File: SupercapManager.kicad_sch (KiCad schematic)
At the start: 0 parts

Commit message: Add subsheets
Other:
- added sheet Current Sense (isense.kicad_sch)
- added sheet Input Buck & Charger (buck.kicad_sch)
- added sheet Output Boost (boost.kicad_sch)
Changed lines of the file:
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@@
 		(comment 1 "Robomaster")
+	)
+	(sheet
+		(at 81.28 97.79)
+		(size 25.4 15.24)
+		(fields_autoplaced yes)
+		(stroke
+			(width 0.1524)
+			(type solid)
+		)
+		(fill
+			(color 0 0 0 0.0000)
+		)
+		(property "Sheetname" "Input Buck & Charger"
+			(at 81.28 97.0784 0)
+			(effects
+				(font
+					(size 1.27 1.27)
+				)
+				(justify left bottom)
+			)
+		)
+		(property "Sheetfile" "buck.kicad_sch"
+			(at 81.28 113.6146 0)
+			(effects
+				(font
+					(size 1.27 1.27)
+				)
+				(justify left top)
+			)
+		)
+		(instances
+			(project "SupercapManager"
+				(path "/6197145b-e7d4-44cc-9d90-537b6501bf60"
+					(page "2")
+				)
+			)
+		)
+	)
+	(sheet
+		(at 118.11 73.66)
+		(size 26.67 12.7)
+		(fields_autoplaced yes)
+		(stroke
+			(width 0.1524)
+			(type solid)
+		)
+		(fill
+			(color 0 0 0 0.0000)
+		)
+		(property "Sheetname" "Current Sense"
+			(at 118.11 72.9484 0)
+			(effects
+				(font
+					(size 1.27 1.27)
+				)
+				(justify left bottom)
+			)
+		)
+		(property "Sheetfile" "isense.kicad_sch"
+			(at 118.11 86.9446 0)
+			(effects
+				(font
+					(size 1.27 1.27)
+				)
+				(justify left top)
+			)
+		)
+		(instances
+			(project "SupercapManager"
+				(path "/6197145b-e7d4-44cc-9d90-537b6501bf60"
+					(page "4")
+				)
+			)
+		)
+	)
+	(sheet
+		(at 162.56 97.79)
+		(size 26.67 15.24)
+		(fields_autoplaced yes)
+		(stroke
+			(width 0.1524)
+			(type solid)
+		)
+		(fill
+			(color 0 0 0 0.0000)
+		)
+		(property "Sheetname" "Output Boost"
+			(at 162.56 97.0784 0)
+			(effects
+				(font
+					(size 1.27 1.27)
+				)
+				(justify left bottom)
+			)
+		)
+		(property "Sheetfile" "boost.kicad_sch"
+			(at 162.56 113.6146 0)
+			(effects
+				(font
+					(size 1.27 1.27)
+				)
+				(justify left top)
+			)
+		)
+		(instances
+			(project "SupercapManager"
+				(path "/6197145b-e7d4-44cc-9d90-537b6501bf60"
+					(page "3")
+				)
+			)
+		)
 	)
 	(sheet_instances

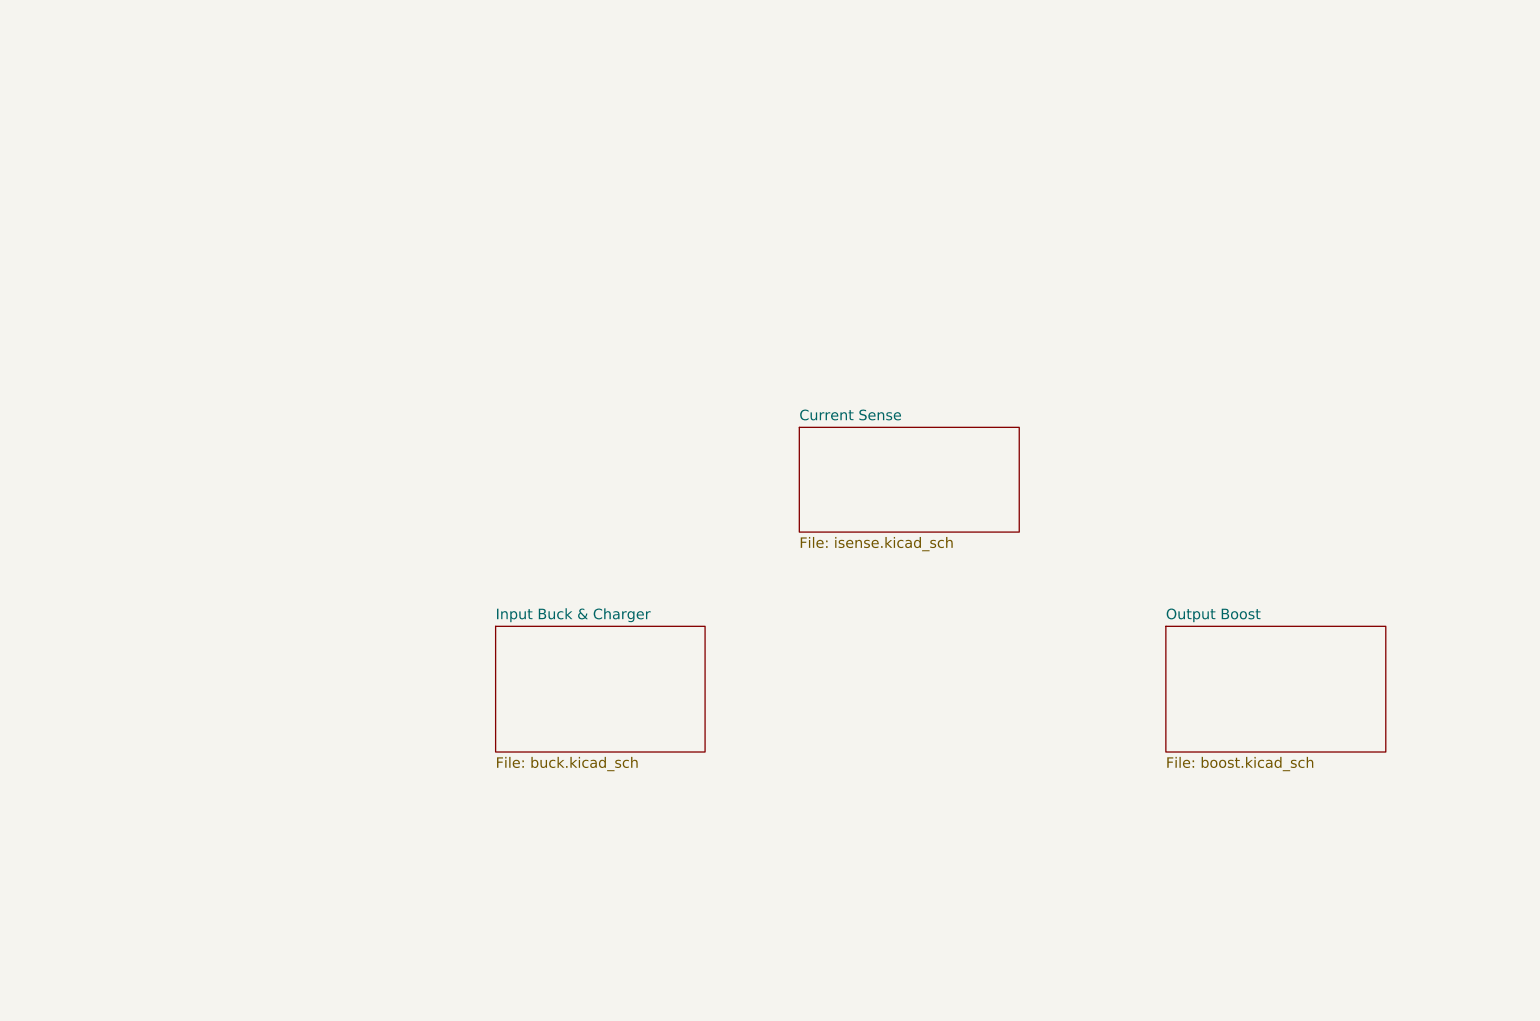
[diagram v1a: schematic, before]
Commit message: Added some text in the subsheets to outline what needs to be added inside of each subsheet
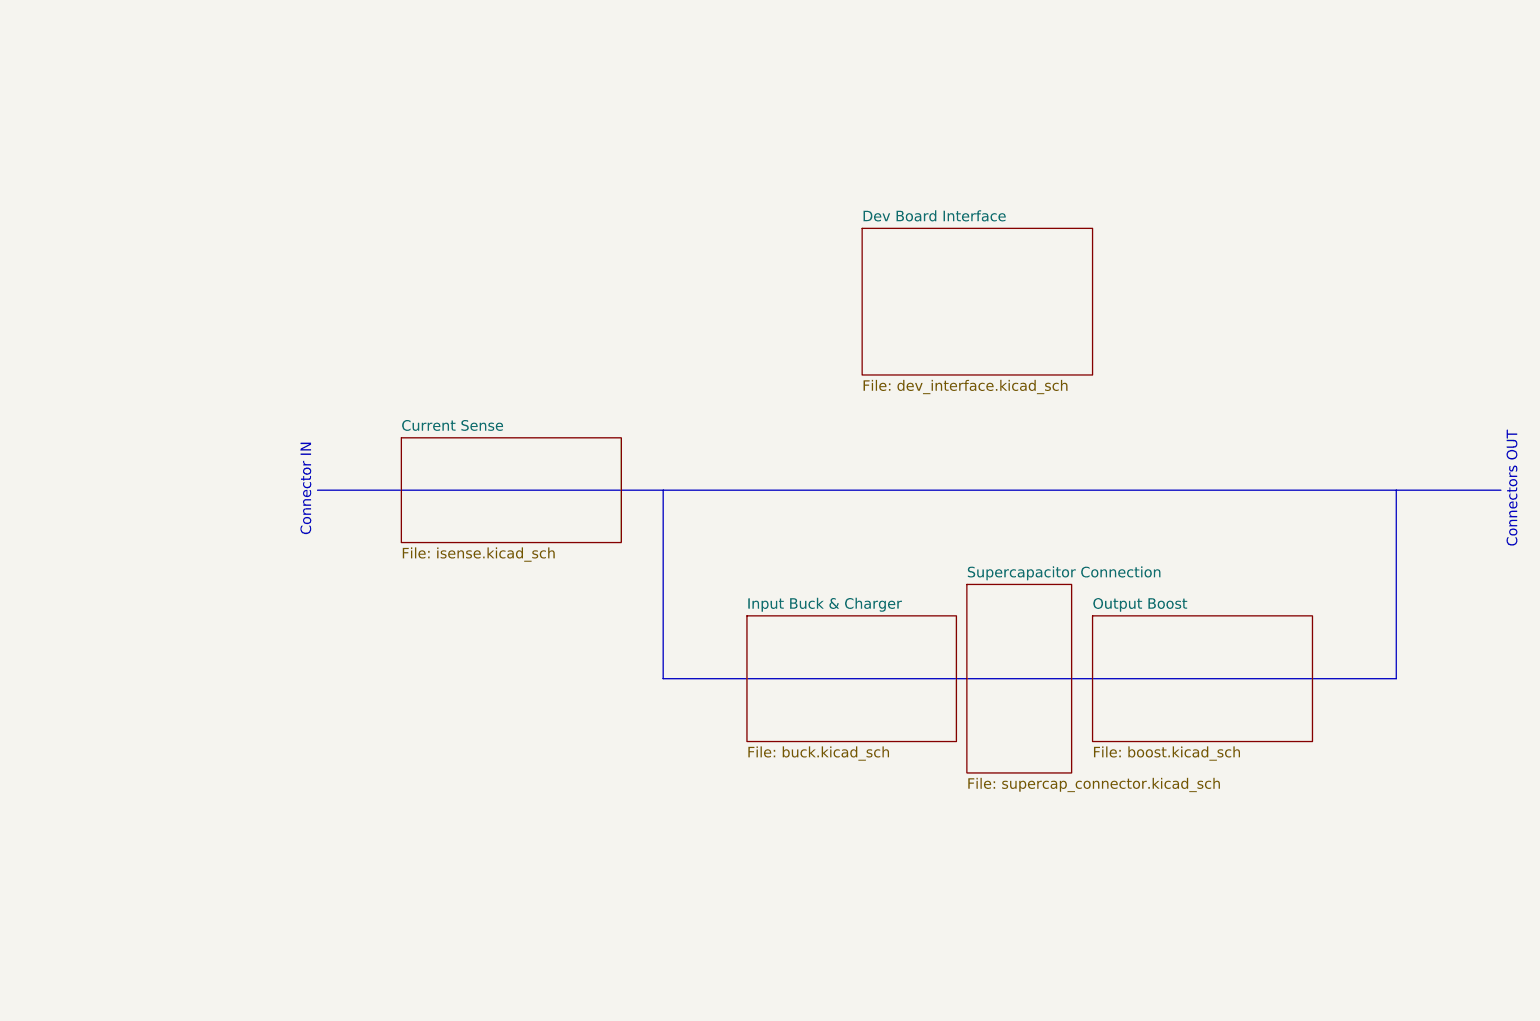
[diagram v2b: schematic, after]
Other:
- added sheet Dev Board Interface (dev_interface.kicad_sch)
- added sheet Supercapacitor Connection (supercap_connector.kicad_sch)
- note added: "Connector IN"
- note added: "Connectors OUT"
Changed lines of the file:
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@@
 		(comment 1 "Robomaster")
 	)
-	(sheet
-		(at 81.28 97.79)
+	(polyline
+		(pts
+			(xy 101.6 81.28) (xy 101.6 104.14)
+		)
+		(stroke
+			(width 0)
+			(type default)
+		)
+	)
+	(polyline
+		(pts
+			(xy 101.6 104.14) (xy 190.5 104.14)
+		)
+		(stroke
+			(width 0)
+			(type default)
+		)
+	)
+	(polyline
+		(pts
+			(xy 59.69 81.28) (xy 203.2 81.28)
+		)
+		(stroke
+			(width 0)
+			(type default)
+		)
+	)
+	(polyline
+		(pts
+			(xy 190.5 104.14) (xy 190.5 81.28)
+		)
+		(stroke
+			(width 0)
+			(type default)
+		)
+	)
+	(text "Connector IN"
+		(exclude_from_sim no)
+		(at 59.055 81.28 90)
+		(effects
+			(font
+				(size 1.27 1.27)
+			)
+			(justify bottom)
+		)
+	)
+	(text "Connectors OUT"
+		(exclude_from_sim no)
+		(at 203.835 81.28 90)
+		(effects
+			(font
+				(size 1.27 1.27)
+			)
+			(justify top)
+		)
+	)
+	(sheet
+		(at 125.73 49.53)
+		(size 27.94 17.78)
+		(fields_autoplaced yes)
+		(stroke
+			(width 0.1524)
+			(type solid)
+		)
+		(fill
+			(color 0 0 0 0.0000)
+		)
+		(property "Sheetname" "Dev Board Interface"
+			(at 125.73 48.8184 0)
+			(effects
+				(font
+					(size 1.27 1.27)
+				)
+				(justify left bottom)
+			)
+		)
+		(property "Sheetfile" "dev_interface.kicad_sch"
+			(at 125.73 67.8946 0)
+			(effects
+				(font
+					(size 1.27 1.27)
+				)
+				(justify left top)
+			)
+		)
+		(instances
+			(project "SupercapManager"
+				(path "/6197145b-e7d4-44cc-9d90-537b6501bf60"
+					(page "5")
+				)
+			)
+		)
+	)
+	(sheet
+		(at 111.76 96.52)
 		(size 25.4 15.24)
 		(fields_autoplaced yes)
@@
 		)
 		(property "Sheetname" "Input Buck & Charger"
-			(at 81.28 97.0784 0)
+			(at 111.76 95.8084 0)
 			(effects
 				(font
@@
 		)
 		(property "Sheetfile" "buck.kicad_sch"
-			(at 81.28 113.6146 0)
+			(at 111.76 112.3446 0)
 			(effects
 				(font
@@
 	)
 	(sheet
-		(at 118.11 73.66)
+		(at 138.43 92.71)
+		(size 12.7 22.86)
+		(fields_autoplaced yes)
+		(stroke
+			(width 0.1524)
+			(type solid)
+		)
+		(fill
+			(color 0 0 0 0.0000)
+		)
+		(property "Sheetname" "Supercapacitor Connection"
+			(at 138.43 91.9984 0)
+			(effects
+				(font
+					(size 1.27 1.27)
+				)
+				(justify left bottom)
+			)
+		)
+		(property "Sheetfile" "supercap_connector.kicad_sch"
+			(at 138.43 116.1546 0)
+			(effects
+				(font
+					(size 1.27 1.27)
+				)
+				(justify left top)
+			)
+		)
+		(instances
+			(project "SupercapManager"
+				(path "/6197145b-e7d4-44cc-9d90-537b6501bf60"
+					(page "6")
+				)
+			)
+		)
+	)
+	(sheet
+		(at 69.85 74.93)
 		(size 26.67 12.7)
 		(fields_autoplaced yes)
@@
 		)
 		(property "Sheetname" "Current Sense"
-			(at 118.11 72.9484 0)
+			(at 69.85 74.2184 0)
 			(effects
 				(font
@@
 		)
 		(property "Sheetfile" "isense.kicad_sch"
-			(at 118.11 86.9446 0)
+			(at 69.85 88.2146 0)
 			(effects
 				(font
@@
 	)
 	(sheet
-		(at 162.56 97.79)
+		(at 153.67 96.52)
 		(size 26.67 15.24)
 		(fields_autoplaced yes)
@@
 		)
 		(property "Sheetname" "Output Boost"
-			(at 162.56 97.0784 0)
+			(at 153.67 95.8084 0)
 			(effects
 				(font
@@
 		)
 		(property "Sheetfile" "boost.kicad_sch"
-			(at 162.56 113.6146 0)
-			(effects
-				(font
+			(at 153.67 112.3446 0)
+			(effects
+				(font

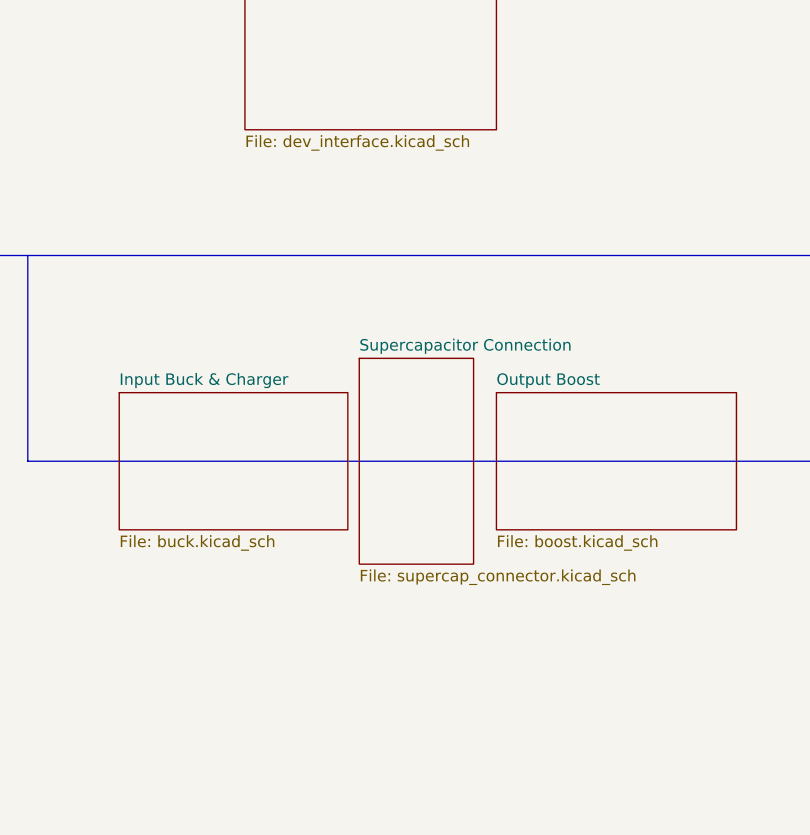
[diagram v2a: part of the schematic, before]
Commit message: Added two more subsheets and updated all text inside
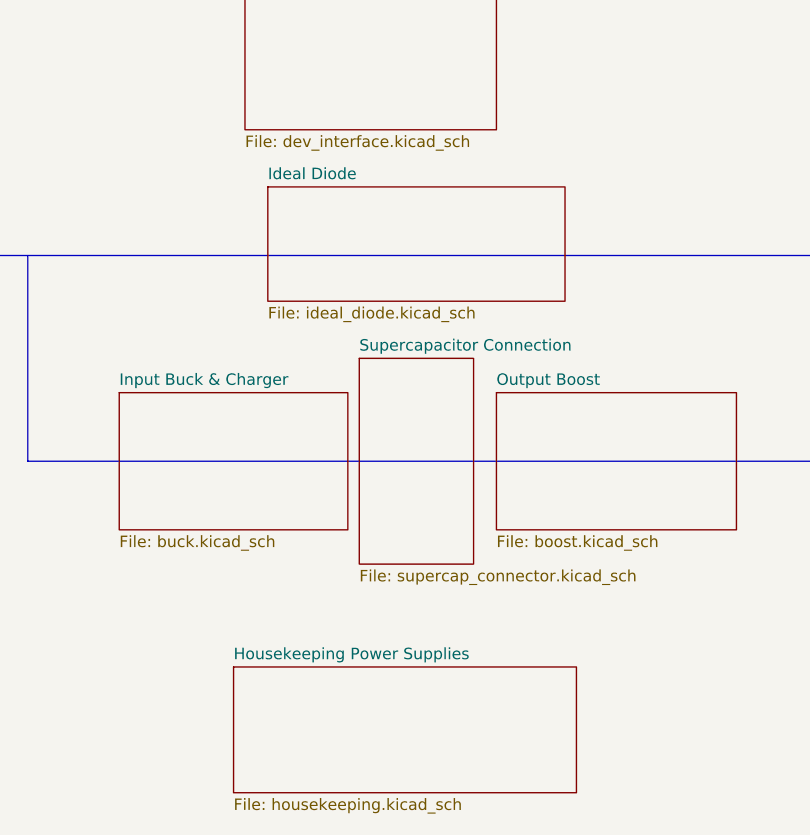
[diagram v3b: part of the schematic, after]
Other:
- added sheet Housekeeping Power Supplies (housekeeping.kicad_sch)
- added sheet Ideal Diode (ideal_diode.kicad_sch)
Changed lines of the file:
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@@
+	)
+	(sheet
+		(at 124.46 127)
+		(size 38.1 13.97)
+		(fields_autoplaced yes)
+		(stroke
+			(width 0.1524)
+			(type solid)
+		)
+		(fill
+			(color 0 0 0 0.0000)
+		)
+		(property "Sheetname" "Housekeeping Power Supplies"
+			(at 124.46 126.2884 0)
+			(effects
+				(font
+					(size 1.27 1.27)
+				)
+				(justify left bottom)
+			)
+		)
+		(property "Sheetfile" "housekeeping.kicad_sch"
+			(at 124.46 141.5546 0)
+			(effects
+				(font
+					(size 1.27 1.27)
+				)
+				(justify left top)
+			)
+		)
+		(instances
+			(project "SupercapManager"
+				(path "/6197145b-e7d4-44cc-9d90-537b6501bf60"
+					(page "8")
+				)
+			)
+		)
 	)
 	(sheet
@@
 				)
 			)
+		)
+	)
+	(sheet
+		(at 128.27 73.66)
+		(size 33.02 12.7)
+		(fields_autoplaced yes)
+		(stroke
+			(width 0.1524)
+			(type solid)
+		)
+		(fill
+			(color 0 0 0 0.0000)
+		)
+		(property "Sheetname" "Ideal Diode"
+			(at 128.27 72.9484 0)
+			(effects
+				(font
+					(size 1.27 1.27)
+				)
+				(justify left bottom)
+			)
+		)
+		(property "Sheetfile" "ideal_diode.kicad_sch"
+			(at 128.27 86.9446 0)
+			(effects
+				(font
+					(size 1.27 1.27)
+				)
+				(justify left top)
+			)
+		)
+		(instances
+			(project "SupercapManager"
+				(path "/6197145b-e7d4-44cc-9d90-537b6501bf60"
+					(page "7")
+				)
+			)

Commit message: Added in & out data from each subsheet
For more details, please contact @leftisttachyon on Discord
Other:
- removed sheet Supercapacitor Connection
- note added: "Connectors to & from supercap + SCMM"
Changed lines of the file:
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@@
+		)
+	)
+	(text "Connectors to &\nfrom supercap + SCMM"
+		(exclude_from_sim no)
+		(at 145.542 104.394 90)
+		(effects
+			(font
+				(size 1.27 1.27)
+			)
+			(justify bottom)
 		)
 	)
 	(sheet
-		(at 125.73 49.53)
+		(at 129.54 46.99)
 		(size 27.94 17.78)
 		(fields_autoplaced yes)
@@
 		)
 		(property "Sheetname" "Dev Board Interface"
-			(at 125.73 48.8184 0)
+			(at 129.54 46.2784 0)
 			(effects
 				(font
@@
 		)
 		(property "Sheetfile" "dev_interface.kicad_sch"
-			(at 125.73 67.8946 0)
+			(at 129.54 65.3546 0)
 			(effects
 				(font
@@
 				)
 			)
-		)
-	)
-	(sheet
-		(at 138.43 92.71)
-		(size 12.7 22.86)
-		(fields_autoplaced yes)
-		(stroke
-			(width 0.1524)
-			(type solid)
-		)
-		(fill
-			(color 0 0 0 0.0000)
-		)
-		(property "Sheetname" "Supercapacitor Connection"
-			(at 138.43 91.9984 0)
-			(effects
-				(font
-					(size 1.27 1.27)
-				)
-				(justify left bottom)
-			)
-		)
-		(property "Sheetfile" "supercap_connector.kicad_sch"
-			(at 138.43 116.1546 0)
-			(effects
-				(font
-					(size 1.27 1.27)
-				)
-				(justify left top)
-			)
-		)
-		(instances
-			(project "SupercapManager"
-				(path "/6197145b-e7d4-44cc-9d90-537b6501bf60"
-					(page "6")
-				)
-			)

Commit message: Completed first version of housekeeping supplies
+5V and +3V3 from mini PC +24V
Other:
- company: UT Stampede -> UT Robomaster
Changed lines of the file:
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@@
 	(title_block
 		(title "Supercapacitor Manager")
-		(date "2024-10-18")
+		(date "2024-11-15")
 		(rev "1")
-		(company "UT Stampede")
+		(company "UT Robomaster")
 		(comment 1 "Robomaster")
 	)

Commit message: Selected an ideal diode
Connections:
- no-connect marks 0 -> 2
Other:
- note added: "Chassis (power) ground"
- note added: "GND reference:"
- note added: "Mini PC ground"
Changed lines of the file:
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@@
 		(comment 1 "Robomaster")
 	)
+	(no_connect
+		(at 27.94 29.21)
+	)
+	(no_connect
+		(at 27.94 36.83)
+	)
 	(polyline
 		(pts
@@
 		)
 	)
+	(text "GND reference:"
+		(exclude_from_sim no)
+		(at 34.29 25.4 0)
+		(effects
+			(font
+				(size 1.27 1.27)
+			)
+			(justify left)
+		)
+	)
 	(text "Connectors to &\nfrom supercap + SCMM"
 		(exclude_from_sim no)
@@
 		)
 	)
+	(text "Chassis (power) ground"
+		(exclude_from_sim no)
+		(at 34.29 31.115 0)
+		(effects
+			(font
+				(size 1.27 1.27)
+			)
+			(justify left)
+		)
+	)
+	(text "Mini PC ground"
+		(exclude_from_sim no)
+		(at 34.29 38.735 0)
+		(effects
+			(font
+				(size 1.27 1.27)
+			)
+			(justify left)
+		)
+	)
+	(symbol
+		(lib_id "power:GND")
+		(at 27.94 36.83 0)
+		(unit 1)
+		(exclude_from_sim no)
+		(in_bom yes)
+		(on_board yes)
+		(dnp no)
+		(fields_autoplaced yes)
+		(property "Reference" "#PWR06"
+			(at 27.94 43.18 0)
+			(effects
+				(font
+					(size 1.27 1.27)
+				)
+				(hide yes)
+			)
+		)
+		(property "Value" "GND"
+			(at 27.94 41.91 0)
+			(effects
+				(font
+					(size 1.27 1.27)
+				)
+			)
+		)
+		(property "Footprint" ""
+			(at 27.94 36.83 0)
+			(effects
+				(font
+					(size 1.27 1.27)
+				)
+				(hide yes)
+			)
+		)
+		(property "Datasheet" ""
+			(at 27.94 36.83 0)
+			(effects
+				(font
+					(size 1.27 1.27)
+				)
+				(hide yes)
+			)
+		)
+		(property "Description" "Power symbol creates a global label with name \"GND\" , ground"
+			(at 27.94 36.83 0)
+			(effects
+				(font
+					(size 1.27 1.27)
+				)
+				(hide yes)
+			)
+		)
+		(pin "1"
+		)
+		(instances
+			(project ""
+				(path "/6197145b-e7d4-44cc-9d90-537b6501bf60"
+					(reference "#PWR06")
+					(unit 1)
+				)
+			)
+		)
+	)
+	(symbol
+		(lib_id "power:GNDPWR")
+		(at 27.94 29.21 0)
+		(unit 1)
+		(exclude_from_sim no)
+		(in_bom yes)
+		(on_board yes)
+		(dnp no)
+		(fields_autoplaced yes)
+		(property "Reference" "#PWR05"
+			(at 27.94 34.29 0)
+			(effects
+				(font
+					(size 1.27 1.27)
+				)
+				(hide yes)
+			)
+		)
+		(property "Value" "GNDPWR"
+			(at 27.813 33.02 0)
+			(effects
+				(font
+					(size 1.27 1.27)
+				)
+			)
+		)
+		(property "Footprint" ""
+			(at 27.94 30.48 0)
+			(effects
+				(font
+					(size 1.27 1.27)
+				)
+				(hide yes)
+			)
+		)
+		(property "Datasheet" ""
+			(at 27.94 30.48 0)
+			(effects
+				(font
+					(size 1.27 1.27)
+				)
+				(hide yes)
+			)
+		)
+		(property "Description" "Power symbol creates a global label with name \"GNDPWR\" , global ground"
+			(at 27.94 29.21 0)
+			(effects
+				(font
+					(size 1.27 1.27)
+				)
+				(hide yes)
+			)
+		)
+		(pin "1"
+		)
+		(instances
+			(project ""
+				(path "/6197145b-e7d4-44cc-9d90-537b6501bf60"
+					(reference "#PWR05")
+					(unit 1)
+				)
+			)
+		)
+	)

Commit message: Selected components for ideal diode and DACs
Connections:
- no-connect marks 2 -> 3
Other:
- note added: "Dev board ground"
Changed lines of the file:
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@@
 		(at 27.94 36.83)
+	)
+	(no_connect
+		(at 27.94 46.99)
 	)
 	(polyline
@@
 		)
 	)
+	(text "Dev board ground"
+		(exclude_from_sim no)
+		(at 33.655 48.895 0)
+		(effects
+			(font
+				(size 1.27 1.27)
+			)
+			(justify left)
+		)
+	)
 	(text "Chassis (power) ground"
 		(exclude_from_sim no)
@@
 		)
 	)
+	(symbol
+		(lib_id "power:GNDD")
+		(at 27.94 46.99 0)
+		(unit 1)
+		(exclude_from_sim no)
+		(in_bom yes)
+		(on_board yes)
+		(dnp no)
+		(fields_autoplaced yes)
+		(property "Reference" "#PWR08"
+			(at 27.94 53.34 0)
+			(effects
+				(font
+					(size 1.27 1.27)
+				)
+				(hide yes)
+			)
+		)
+		(property "Value" "GNDD"
+			(at 27.94 50.8 0)
+			(effects
+				(font
+					(size 1.27 1.27)
+				)
+			)
+		)
+		(property "Footprint" ""
+			(at 27.94 46.99 0)
+			(effects
+				(font
+					(size 1.27 1.27)
+				)
+				(hide yes)
+			)
+		)
+		(property "Datasheet" ""
+			(at 27.94 46.99 0)
+			(effects
+				(font
+					(size 1.27 1.27)
+				)
+				(hide yes)
+			)
+		)
+		(property "Description" "Power symbol creates a global label with name \"GNDD\" , digital ground"
+			(at 27.94 46.99 0)
+			(effects
+				(font
+					(size 1.27 1.27)
+				)
+				(hide yes)
+			)
+		)
+		(pin "1"
+		)
+		(instances
+			(project ""
+				(path "/6197145b-e7d4-44cc-9d90-537b6501bf60"
+					(reference "#PWR08")
+					(unit 1)
+				)
+			)
+		)
+	)

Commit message: Finish Dev board interface
sorry morris
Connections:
- no-connect marks 3 -> 5
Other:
- sheet Current Sense ports: added CHARGING_EN, CURR, DIRECT_EN, PWR_{IN}, PWR_{OUT}; removed none
- sheet Housekeeping Power Supplies ports: added +24_{MiniPC}, +3V3, +5V; removed none
- note added: "+3.3V to Mini PC GND"
- note added: "PWR reference:"
